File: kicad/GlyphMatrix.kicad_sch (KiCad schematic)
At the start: 36 parts, among them J1 Conn_01x04, SW1 SW_Push, SW2 SW_Push, U1 W25Q128JVS, U2 USBLC6-2SC6, U3 XC6206PxxxMR-Regulator_Linear, Y1 12MHz

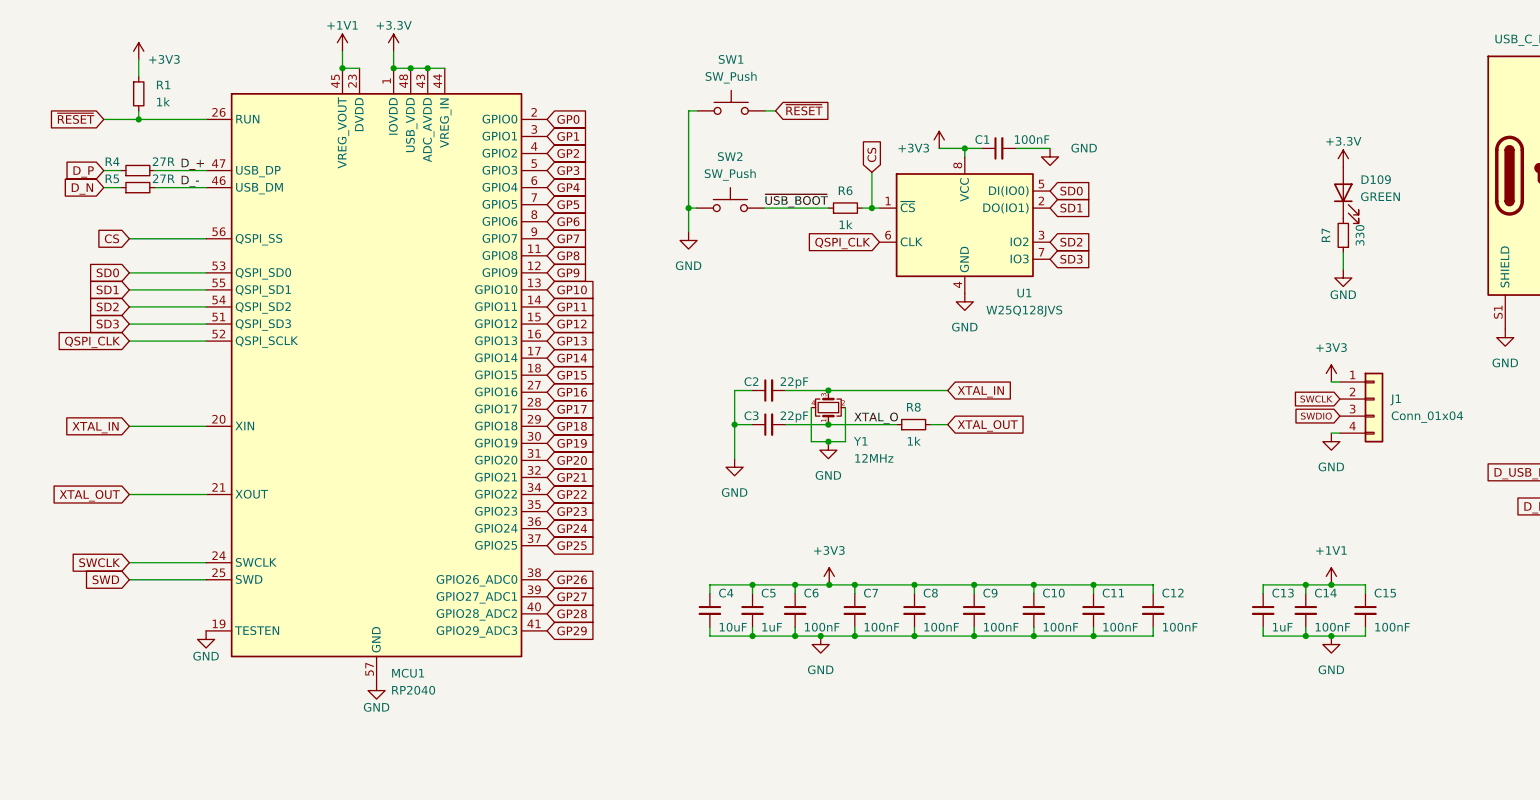
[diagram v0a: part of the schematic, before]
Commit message: added MCU
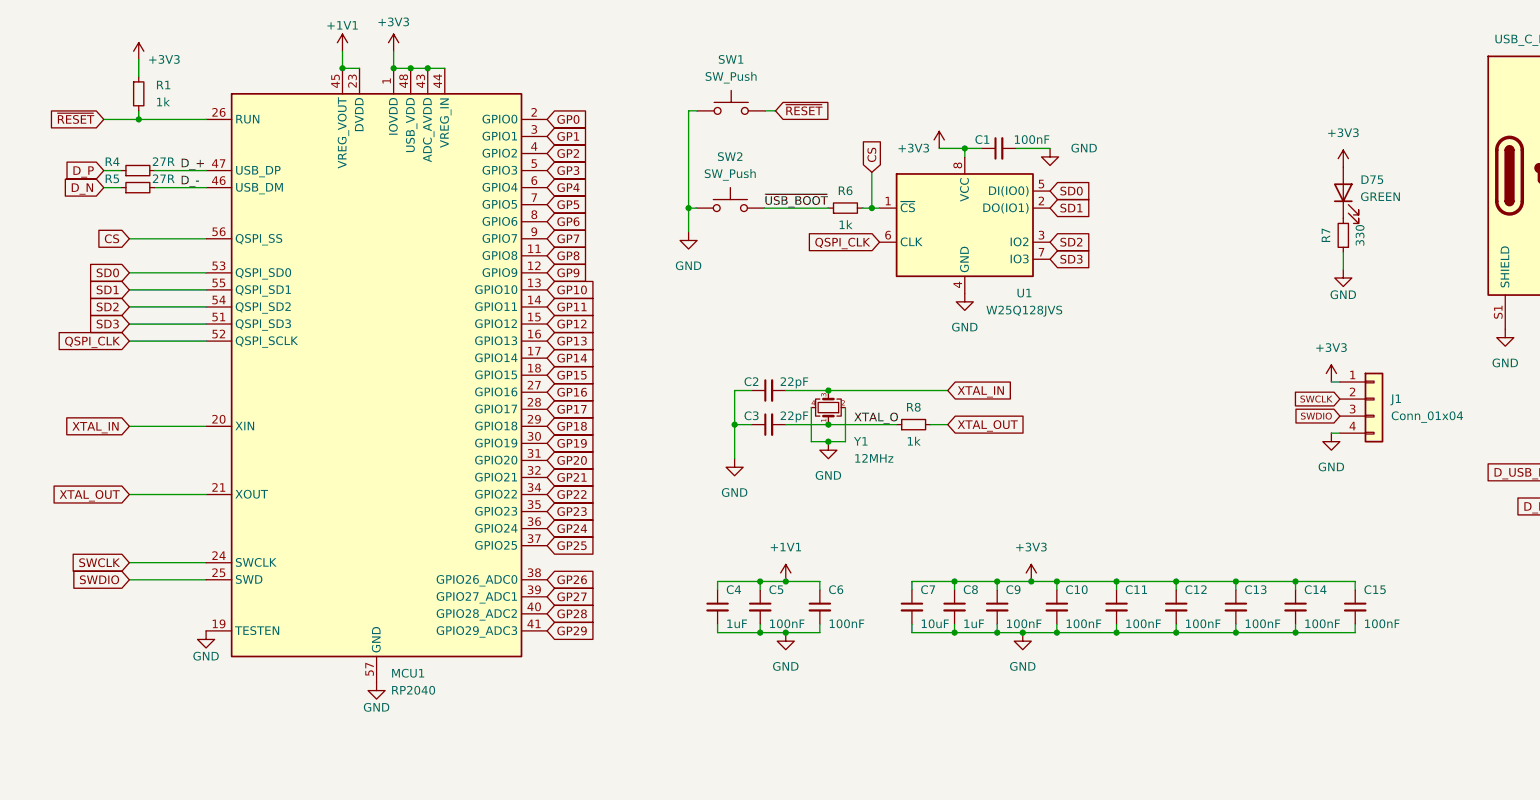
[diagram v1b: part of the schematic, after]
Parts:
- renumbered C7 to C10, C8 to C11, C9 to C12, C10 to C13, C11 to C14, C12 to C15, C13 to C4, C14 to C5, C15 to C6, C4 to C7, C5 to C8, C6 to C9, D109 to D75
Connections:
- net +3.3V is gone; now on net +3V3: D75.2 (A), MCU1.1 (IOVDD), MCU1.10 (IOVDD), MCU1.22 (IOVDD), MCU1.33 (IOVDD), MCU1.42 (IOVDD), MCU1.43 (ADC_AVDD), MCU1.44 (VREG_IN), MCU1.48 (USB_VDD), MCU1.49 (IOVDD)
- net SWD is gone; now on net SWDIO: MCU1.25 (SWD)
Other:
- moved on the sheet: C10, C11, C12, C13, C14, C15, C4, C5, C6, C7, C8, C9

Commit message: pogo pin connectors
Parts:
- renumbered D75 to LED1
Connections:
- net GP0 renamed SCR
- net GP1 renamed NUM
- net GP10 renamed ROW04
- net GP11 renamed ROW03
- net GP12 renamed ROW02
- net GP13 renamed ROW01
- net GP14 renamed ROW00
- net GP15 renamed CAPS
- net GP16 renamed COL0
- net GP17 renamed COL1
- net GP18 renamed COL2
- net GP19 renamed COL3
- net GP2 renamed ROW17
- net GP20 renamed COL4
- net GP21 renamed COL5
- net GP22 renamed COL6
- net GP23 renamed ROW06
- net GP24 renamed ROW07
- net GP25 renamed ROW08
- net GP26 renamed ROW09
- net GP27 renamed ROW10
- net GP28 renamed ROW11
- net GP3 renamed ROW16
- net GP4 renamed ROW15
- net GP5 renamed ROW14
- net GP6 renamed ROW13
- net GP7 renamed ROW12
- net GP8 renamed RGB
- net GP9 renamed ROW05
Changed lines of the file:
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@@
 		)
 	)
-	(global_label "GP17"
+	(global_label "COL1"
 		(shape input)
 		(at 88.392 77.978 0)
@@
 		)
 		(property "Intersheetrefs" "${INTERSHEET_REFS}"
-			(at 94.8885 77.978 0)
+			(at 96.2153 77.978 0)
 			(effects
 				(font
@@
 		)
 	)
-	(global_label "GP8"
+	(global_label "RGB"
 		(shape input)
 		(at 88.392 55.118 0)
@@
 		)
 		(property "Intersheetrefs" "${INTERSHEET_REFS}"
-			(at 94.8885 55.118 0)
+			(at 95.1872 55.118 0)
 			(effects
 				(font
@@
 		)
 	)
-	(global_label "GP16"
+	(global_label "COL0"
 		(shape input)
 		(at 88.392 75.438 0)
@@
 		)
 		(property "Intersheetrefs" "${INTERSHEET_REFS}"
-			(at 94.8885 75.438 0)
+			(at 96.2153 75.438 0)
 			(effects
 				(font
@@
 		)
 	)
-	(global_label "GP6"
+	(global_label "ROW13"
 		(shape input)
 		(at 88.392 50.038 0)
@@
 		)
 		(property "Intersheetrefs" "${INTERSHEET_REFS}"
-			(at 94.8885 50.038 0)
+			(at 97.8481 50.038 0)
 			(effects
 				(font
@@
 		)
 	)
-	(global_label "GP13"
+	(global_label "ROW01"
 		(shape input)
 		(at 88.392 67.818 0)
@@
 		)
 		(property "Intersheetrefs" "${INTERSHEET_REFS}"
-			(at 94.8885 67.818 0)
+			(at 97.8481 67.818 0)
 			(effects
 				(font
@@
 		)
 	)
-	(global_label "GP20"
+	(global_label "COL4"
 		(shape input)
 		(at 88.392 85.598 0)
@@
 		)
 		(property "Intersheetrefs" "${INTERSHEET_REFS}"
-			(at 94.8885 85.598 0)
+			(at 96.2153 85.598 0)
 			(effects
 				(font
@@
 		)
 	)
-	(global_label "GP25"
+	(global_label "ROW08"
 		(shape input)
 		(at 88.392 98.298 0)
@@
 		)
 		(property "Intersheetrefs" "${INTERSHEET_REFS}"
-			(at 94.8885 98.298 0)
+			(at 97.8481 98.298 0)
 			(effects
 				(font
@@
 		)
 	)
-	(global_label "GP2"
+	(global_label "ROW17"
 		(shape input)
 		(at 88.392 39.878 0)
@@
 		)
 		(property "Intersheetrefs" "${INTERSHEET_REFS}"
-			(at 94.8885 39.878 0)
+			(at 97.8481 39.878 0)
 			(effects
 				(font
@@
 		)
 	)
-	(global_label "GP0"
+	(global_label "SCR"
 		(shape input)
 		(at 88.392 34.798 0)
@@
 		)
 		(property "Intersheetrefs" "${INTERSHEET_REFS}"
-			(at 94.8885 34.798 0)
+			(at 95.1267 34.798 0)
 			(effects
 				(font
@@
 		)
 	)
-	(global_label "GP24"
+	(global_label "ROW07"
 		(shape input)
 		(at 88.392 95.758 0)
@@
 		)
 		(property "Intersheetrefs" "${INTERSHEET_REFS}"
-			(at 94.8885 95.758 0)
+			(at 97.8481 95.758 0)
 			(effects
 				(font
@@
 		)
 	)
-	(global_label "GP14"
+	(global_label "ROW00"
 		(shape input)
 		(at 88.392 70.358 0)
@@
 		)
 		(property "Intersheetrefs" "${INTERSHEET_REFS}"
-			(at 94.8885 70.358 0)
+			(at 97.8481 70.358 0)
 			(effects
 				(font
@@
 		)
 	)
-	(global_label "GP9"
+	(global_label "ROW05"
 		(shape input)
 		(at 88.392 57.658 0)
@@
 		)
 		(property "Intersheetrefs" "${INTERSHEET_REFS}"
-			(at 94.8885 57.658 0)
+			(at 97.8481 57.658 0)
 			(effects
 				(font
@@
 		)
 	)
-	(global_label "GP23"
+	(global_label "ROW06"
 		(shape input)
 		(at 88.392 93.218 0)
@@
 		)
 		(property "Intersheetrefs" "${INTERSHEET_REFS}"
-			(at 94.8885 93.218 0)
+			(at 97.8481 93.218 0)
 			(effects
 				(font
@@
 		)
 	)
-	(global_label "GP15"
+	(global_label "CAPS"
 		(shape input)
 		(at 88.392 72.898 0)
@@
 		)
 		(property "Intersheetrefs" "${INTERSHEET_REFS}"
-			(at 94.8885 72.898 0)
+			(at 96.2153 72.898 0)
 			(effects
 				(font
@@
 		)
 	)
-	(global_label "GP28"
+	(global_label "ROW11"
 		(shape input)
 		(at 88.392 108.458 0)
@@
 		)
 		(property "Intersheetrefs" "${INTERSHEET_REFS}"
-			(at 94.8885 108.458 0)
+			(at 97.8481 108.458 0)
 			(effects
 				(font
@@
 		)
 	)
-	(global_label "GP19"
+	(global_label "COL3"
 		(shape input)
 		(at 88.392 83.058 0)
@@
 		)
 		(property "Intersheetrefs" "${INTERSHEET_REFS}"
-			(at 94.8885 83.058 0)
+			(at 96.2153 83.058 0)
 			(effects
 				(font
@@
 		)
 	)
-	(global_label "GP10"
+	(global_label "ROW04"
 		(shape input)
 		(at 88.392 60.198 0)
@@
 		)
 		(property "Intersheetrefs" "${INTERSHEET_REFS}"
-			(at 94.8885 60.198 0)
+			(at 97.8481 60.198 0)
 			(effects
 				(font
@@
 		)
 	)
-	(global_label "GP11"
+	(global_label "ROW03"
 		(shape input)
 		(at 88.392 62.738 0)
@@
 		)
 		(property "Intersheetrefs" "${INTERSHEET_REFS}"
-			(at 94.8885 62.738 0)
+			(at 97.8481 62.738 0)
 			(effects
 				(font
@@
 		)
 	)
-	(global_label "GP7"
+	(global_label "ROW12"
 		(shape input)
 		(at 88.392 52.578 0)
@@
 		)
 		(property "Intersheetrefs" "${INTERSHEET_REFS}"
-			(at 94.8885 52.578 0)
+			(at 97.8481 52.578 0)
 			(effects
 				(font
@@
 		)
 	)
-	(global_label "GP27"
+	(global_label "ROW10"
 		(shape input)
 		(at 88.392 105.918 0)
@@
 		)
 		(property "Intersheetrefs" "${INTERSHEET_REFS}"
-			(at 94.8885 105.918 0)
+			(at 97.8481 105.918 0)
 			(effects
 				(font
@@
 		)
 	)
-	(global_label "GP1"
+	(global_label "NUM"
 		(shape input)
 		(at 88.392 37.338 0)
@@
 		)
 		(property "Intersheetrefs" "${INTERSHEET_REFS}"
-			(at 94.8885 37.338 0)
+			(at 95.4896 37.338 0)
 			(effects
 				(font
@@
 		)
 	)
-	(global_label "GP3"
+	(global_label "ROW16"
 		(shape input)
 		(at 88.392 42.418 0)
@@
 		)
 		(property "Intersheetrefs" "${INTERSHEET_REFS}"
-			(at 94.8885 42.418 0)
+			(at 97.8481 42.418 0)
 			(effects
 				(font
@@
 		)
 	)
-	(global_label "GP4"
+	(global_label "ROW15"
 		(shape input)
 		(at 88.392 44.958 0)
@@
 		)
 		(property "Intersheetrefs" "${INTERSHEET_REFS}"
-			(at 94.8885 44.958 0)
+			(at 97.8481 44.958 0)
 			(effects
 				(font
@@
 		)
 	)
-	(global_label "GP21"
+	(global_label "COL5"
 		(shape input)
 		(at 88.392 88.138 0)
@@
 		)
 		(property "Intersheetrefs" "${INTERSHEET_REFS}"
-			(at 94.8885 88.138 0)
+			(at 96.2153 88.138 0)
 			(effects
 				(font
@@
 		)
 	)
-	(global_label "GP26"
+	(global_label "ROW09"
 		(shape input)
 		(at 88.392 103.378 0)
@@
 		)
 		(property "Intersheetrefs" "${INTERSHEET_REFS}"
-			(at 94.8885 103.378 0)
+			(at 97.8481 103.378 0)
 			(effects
 				(font
@@
 		)
 	)
-	(global_label "GP5"
+	(global_label "ROW14"
 		(shape input)
 		(at 88.392 47.498 0)
@@
 		)
 		(property "Intersheetrefs" "${INTERSHEET_REFS}"
-			(at 94.8885 47.498 0)
+			(at 97.8481 47.498 0)
 			(effects
 				(font
@@
 		)
 	)
-	(global_label "GP18"
+	(global_label "COL2"
 		(shape input)
 		(at 88.392 80.518 0)
@@
 		)
 		(property "Intersheetrefs" "${INTERSHEET_REFS}"
-			(at 94.8885 80.518 0)
+			(at 96.2153 80.518 0)
 			(effects
 				(font
@@
 		)
 	)
-	(global_label "GP22"
+	(global_label "COL6"
 		(shape input)
 		(at 88.392 90.678 0)
@@
 		)
 		(property "Intersheetrefs" "${INTERSHEET_REFS}"
-			(at 94.8885 90.678 0)
+			(at 96.2153 90.678 0)
 			(effects
 				(font
@@
 		)
 	)
-	(global_label "GP12"
+	(global_label "ROW02"
 		(shape input)
 		(at 88.392 65.278 0)
@@
 		)
 		(property "Intersheetrefs" "${INTERSHEET_REFS}"
-			(at 94.8885 65.278 0)
+			(at 97.8481 65.278 0)
 			(effects
 				(font
@@
 		(on_board yes)
 		(dnp no)
-		(property "Reference" "D75"
+		(property "Reference" "LED1"
 			(at 209.55 43.815 90)
 			(effects
@@
 			(project "OmniCode"
 				(path "/c7177d09-71a2-4de7-9a3e-bfc16a7f2797"
-					(reference "D75")
+					(reference "LED1")
 					(unit 1)
 				)

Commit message: screw holes
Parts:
- LED1: value GREEN -> WHITE
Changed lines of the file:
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@@
 			)
 		)
-		(property "Value" "GREEN"
+		(property "Value" "WHITE"
 			(at 209.55 46.355 90)
 			(effects

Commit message: artwork
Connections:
- net CAPS: now also MCU1.11 (GPIO8); no longer MCU1.18 (GPIO15)
- net NUM: now also MCU1.9 (GPIO7); no longer MCU1.3 (GPIO1)
- net RGB: now also MCU1.16 (GPIO13); no longer MCU1.11 (GPIO8)
- net ROW00: now also MCU1.12 (GPIO9); no longer MCU1.17 (GPIO14)
- net ROW01: now also MCU1.13 (GPIO10); no longer MCU1.16 (GPIO13)
- net ROW02: now also MCU1.14 (GPIO11); no longer MCU1.15 (GPIO12)
- net ROW03: now also MCU1.18 (GPIO15); no longer MCU1.14 (GPIO11)
- net ROW04: now also MCU1.17 (GPIO14); no longer MCU1.13 (GPIO10)
- net ROW05: now also MCU1.15 (GPIO12); no longer MCU1.12 (GPIO9)
- net ROW12: now also MCU1.7 (GPIO5); no longer MCU1.9 (GPIO7)
- net ROW13: now also MCU1.6 (GPIO4); no longer MCU1.8 (GPIO6)
- net ROW14: now also MCU1.5 (GPIO3); no longer MCU1.7 (GPIO5)
- net ROW15: now also MCU1.4 (GPIO2); no longer MCU1.6 (GPIO4)
- net ROW16: now also MCU1.3 (GPIO1); no longer MCU1.5 (GPIO3)
- net ROW17: now also MCU1.2 (GPIO0); no longer MCU1.4 (GPIO2)
- net SCR: now also MCU1.8 (GPIO6); no longer MCU1.2 (GPIO0)
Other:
- added sheet RGB (GlyphMatrix-RGB.kicad_sch)
- title: (none) -> RP2040 - Keyboard: OmniCode:9001

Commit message: artwork #2
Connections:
- net COL4: now also MCU1.34 (GPIO22); no longer MCU1.31 (GPIO20)
- net COL6: now also MCU1.31 (GPIO20); no longer MCU1.34 (GPIO22)
- net ROW12: now also MCU1.2 (GPIO0); no longer MCU1.7 (GPIO5)
- net ROW13: now also MCU1.3 (GPIO1); no longer MCU1.6 (GPIO4)
- net ROW14: now also MCU1.4 (GPIO2); no longer MCU1.5 (GPIO3)
- net ROW15: now also MCU1.5 (GPIO3); no longer MCU1.4 (GPIO2)
- net ROW16: now also MCU1.6 (GPIO4); no longer MCU1.3 (GPIO1)
- net ROW17: now also MCU1.7 (GPIO5); no longer MCU1.2 (GPIO0)

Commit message: kibot
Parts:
- LED1: LCSC C84264 -> C965808
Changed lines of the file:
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@@
 			)
 		)
-		(property "LCSC" "C84264"
+		(property "LCSC" "C965808"
 			(at 209.55 43.815 0)
 			(effects

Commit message: reorg schematic (#18)
* GlyphMatrix

* PhaseShift

* DeltaForm
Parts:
- removed C1, C10, C11, C12, C13, C14, C15, C5, C6, C9: 100nF, Capacitor_SMD:C_0402_1005Metric, symbol Device:C_Small
- removed C16, C17, C4, C8: 1uF, Capacitor_SMD:C_0402_1005Metric, symbol Device:C_Small
- removed C2, C3: 22pF, Capacitor_SMD:C_0402_1005Metric, symbol Device:C_Small
- removed C7: 10uF, Capacitor_SMD:C_0402_1005Metric, symbol Device:C_Small
- removed F1: 500mA, Fuse:Fuse_1206_3216Metric, symbol Device:Polyfuse_Small
- removed J1: Conn_01x04, Connector_PinHeader_2.00mm:PinHeader_2x02_P2.00mm_Vertical_SMD, symbol Connector_Generic:Conn_01x04
- removed LED1: WHITE, LED_SMD:LED_0603_1608Metric_Pad1.05x0.95mm_HandSolder, symbol Device:LED
- removed MCU1: RP2040, TB2086_SMD_G:RP2040-QFN-56, symbol MCU_RaspberryPi:RP2040
- removed R1, R6, R8: 1k, Resistor_SMD:R_0402_1005Metric, symbol Device:R_Small
- removed R2, R3: 5k1, Resistor_SMD:R_0402_1005Metric, symbol Device:R_Small
- removed R4, R5: 27R, Resistor_SMD:R_0603_1608Metric, symbol Device:R_Small
- removed R7: 330, Resistor_SMD:R_0603_1608Metric, symbol Device:R_Small
- removed SW1, SW2: SW_Push, Button_Switch_SMD:SW_SPST_SKQG_WithoutStem, symbol Switch:SW_Push
- removed U1: W25Q128JVS, Package_SO:SOIC-8_5.3x5.3mm_P1.27mm, symbol Memory_Flash:W25Q128JVS
- removed U2: USBLC6-2SC6, Package_TO_SOT_SMD:SOT-23-6, symbol Power_Protection:USBLC6-2SC6
- removed U3: XC6206PxxxMR-Regulator_Linear, Package_TO_SOT_SMD:SOT-23, symbol kicad-keyboard-parts:XC6206PxxxMR-Regulator_Linear
- removed USB1: USB_C_Receptacle_USB2.0, TB2086_SMD:GCT_USB4520-03-0-A_REVA, symbol Connector:USB_C_Receptacle_USB2.0
- removed Y1: 12MHz, Crystal:Crystal_SMD_3225-4Pin_3.2x2.5mm, symbol Device:Crystal_GND24_Small
- added D1, D10, D11, D12, D13, D14, D15, D16, D17, D18, D19, D2, D20, D21, D22, D23, D24, D25, D26, D27, D28, D29, D3, D30, D31, D32, D33, D34, D35, D36, D37, D38, D39, D4, D40, D41, D42, D43, D44, D45, D46, D47, D48, D49, D5, D50, D51, D52, D53, D54, D55, D56, D57, D58, D59, D6, D60, D61, D62, D63, D64, D65, D66, D67, D68, D69, D7, D70, D71, D72, D73, D74, D8, D9: 1N4148W, TB2086_SMD:D3_SMD, symbol Device:D
- added H1, H2, H3, H4, H5, H6, H7, H8: MountingHole_Pad, TB2086_MISC:MountingHole_2.2mm_M2_Pad, symbol TB2086_MISC:MountingHole_Pad
- added LED2: GREEN, LED_SMD:LED_0603_1608Metric_Pad1.05x0.95mm_HandSolder, symbol Device:LED
- added POGO1, POGO2: Conn_01x05, TB2086_MISC:Pogopin_1x05_P2.54mm_Curved, symbol Connector_Generic:Conn_01x05
- added POGO3, POGO4, POGO5, POGO6: Conn_01x07, TB2086_MISC:Pogopin_1x07_P2.54mm_Curved, symbol Connector_Generic:Conn_01x07
- added R9: 330, Resistor_SMD:R_0603_1608Metric, symbol Device:R_Small
- added S1, S10, S11, S12, S13, S14, S15, S16, S17, S18, S19, S2, S20, S21, S22, S23, S24, S25, S26, S27, S28, S29, S3, S30, S31, S32, S33, S34, S35, S36, S37, S38, S39, S4, S40, S41, S42, S43, S44, S45, S46, S47, S48, S49, S5, S50, S51, S52, S53, S54, S55, S56, S57, S58, S59, S6, S60, S61, S62, S63, S7, S8, S9: SW_MX_HS, TB2086_KEYSWITCH:SW_MX_HS_1u, symbol TB2086_KEYSWITCH:SW_MX_HS
- added S64: SW_MX_HS, TB2086_KEYSWITCH:SW_MX_HS_1.25u, symbol TB2086_KEYSWITCH:SW_MX_HS
- added S65, S66: SW_MX_HS, TB2086_KEYSWITCH:SW_MX_HS_1.5u, symbol TB2086_KEYSWITCH:SW_MX_HS
- added S67, S68, S69: SW_MX_HS, TB2086_KEYSWITCH:SW_MX_HS_1.75u, symbol TB2086_KEYSWITCH:SW_MX_HS
- added S70: SW_MX_HS, TB2086_KEYSWITCH:SW_MX_HS_2u, symbol TB2086_KEYSWITCH:SW_MX_HS
- added S71, S72: SW_MX_HS, TB2086_KEYSWITCH:SW_MX_HS_2.25u, symbol TB2086_KEYSWITCH:SW_MX_HS
- added S73: SW_MX_HS, TB2086_KEYSWITCH:SW_MX_HS_2.75u, symbol TB2086_KEYSWITCH:SW_MX_HS
- added S74: SW_MX_HS, TB2086_KEYSWITCH:SW_MX_HS_6.25u, symbol TB2086_KEYSWITCH:SW_MX_HS
- added STB1, STB2, STB3, STB4: Stabilizer_Cherry_MX_2.00u, Stabilizer_Cherry_MX_2.00u, symbol PCM_marbastlib-mx:MX_stab
- added STB5: Stabilizer_Cherry_MX_6.25u, Stabilizer_Cherry_MX_6.25u, symbol PCM_marbastlib-mx:MX_stab
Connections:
- net +5V: now also POGO1.4 (Pin_4), POGO2.2 (Pin_2)
- net CAPS: now also LED2.2 (A)
- net COL0: now also POGO3.1 (Pin_1), POGO4.7 (Pin_7), S1.2, S13.2, S14.2, S65.2, S66.2, S67.2, S68.2, S69.2, S70.2, S71.2, S72.2, S73.2
- net COL1: now also POGO3.2 (Pin_2), POGO4.6 (Pin_6), S12.2, S15.2, S26.2, S27.2, S38.2, S39.2, S50.2, S60.2
- net COL2: now also POGO3.3 (Pin_3), POGO4.5 (Pin_5), S11.2, S16.2, S2.2, S25.2, S28.2, S37.2, S40.2, S49.2, S51.2, S63.2, S64.2
- net COL3: now also POGO3.4 (Pin_4), POGO4.4 (Pin_4), S10.2, S17.2, S24.2, S29.2, S3.2, S36.2, S41.2, S48.2, S52.2, S59.2, S62.2
- net COL4: now also POGO3.7 (Pin_7), POGO4.1 (Pin_1), S18.2, S23.2, S30.2, S35.2, S4.2, S42.2, S47.2, S53.2, S58.2, S61.2, S9.2
- net COL5: now also POGO3.6 (Pin_6), POGO4.2 (Pin_2), S19.2, S22.2, S31.2, S34.2, S43.2, S46.2, S5.2, S54.2, S57.2, S74.2, S8.2
- net COL6: now also POGO3.5 (Pin_5), POGO4.3 (Pin_3), S20.2, S21.2, S32.2, S33.2, S44.2, S45.2, S55.2, S56.2, S6.2, S7.2
- net GND: now also H1.1, H2.1, H3.1, H4.1, H5.1, H6.1, H7.1, H8.1, POGO1.5 (Pin_5), POGO2.1 (Pin_1), R9.1
- net NUM: now also POGO1.3 (Pin_3), POGO2.3 (Pin_3)
- net ROW00: now also D1.1 (K), D2.1 (K), D3.1 (K), D4.1 (K), D5.1 (K), D6.1 (K)
- net ROW01: now also D14.1 (K), D15.1 (K), D16.1 (K), D17.1 (K), D18.1 (K), D19.1 (K), D20.1 (K)
- net ROW02: now also D27.1 (K), D28.1 (K), D29.1 (K), D30.1 (K), D31.1 (K), D32.1 (K), D65.1 (K)
- net ROW03: now also D39.1 (K), D40.1 (K), D41.1 (K), D42.1 (K), D43.1 (K), D44.1 (K), D67.1 (K)
- net ROW04: now also D50.1 (K), D51.1 (K), D52.1 (K), D53.1 (K), D54.1 (K), D55.1 (K), D72.1 (K)
- net ROW05: now also D60.1 (K), D64.1 (K), D68.1 (K), D74.1 (K)
- net ROW06: now also D10.1 (K), D11.1 (K), D12.1 (K), D13.1 (K), D7.1 (K), D8.1 (K), D9.1 (K)
- net ROW07: now also D21.1 (K), D22.1 (K), D23.1 (K), D24.1 (K), D25.1 (K), D26.1 (K), D70.1 (K)
- net ROW08: now also D33.1 (K), D34.1 (K), D35.1 (K), D36.1 (K), D37.1 (K), D38.1 (K), D66.1 (K)
- net ROW09: now also D45.1 (K), D46.1 (K), D47.1 (K), D48.1 (K), D49.1 (K), D71.1 (K)
- net ROW10: now also D56.1 (K), D57.1 (K), D58.1 (K), D59.1 (K), D73.1 (K)
- net ROW11: now also D61.1 (K), D62.1 (K), D63.1 (K), D69.1 (K)
- net ROW12: now also POGO5.1 (Pin_1), POGO6.7 (Pin_7)
- net ROW13: now also POGO5.2 (Pin_2), POGO6.6 (Pin_6)
- net ROW14: now also POGO5.3 (Pin_3), POGO6.5 (Pin_5)
- net ROW15: now also POGO5.4 (Pin_4), POGO6.4 (Pin_4)
- net ROW16: now also POGO5.5 (Pin_5), POGO6.3 (Pin_3)
- net ROW17: now also POGO5.6 (Pin_6), POGO6.2 (Pin_2)
- net SCR: now also POGO1.2 (Pin_2), POGO2.4 (Pin_4)
- new net: D23.2 (A), S23.1
- new net: D21.2 (A), S21.1
- new net: D34.2 (A), S34.1
- new net: D30.2 (A), S30.1
- new net: D11.2 (A), S11.1
- new net: D27.2 (A), S27.1
- new net: D2.2 (A), S2.1
- new net: D63.2 (A), S63.1
- new net: D71.2 (A), S71.1
- new net: D16.2 (A), S16.1
- new net: D66.2 (A), S66.1
- new net: D41.2 (A), S41.1
- new net: D39.2 (A), S39.1
- new net: D69.2 (A), S69.1
- new net: D19.2 (A), S19.1
- new net: D32.2 (A), S32.1
- new net: D46.2 (A), S46.1
- new net: D53.2 (A), S53.1
- new net: D54.2 (A), S54.1
- new net: D26.2 (A), S26.1
- new net: D59.2 (A), S59.1
- new net: D14.2 (A), S14.1
- new net: D9.2 (A), S9.1
- new net: D15.2 (A), S15.1
- new net: D67.2 (A), S67.1
- new net: D64.2 (A), S64.1
- new net: D73.2 (A), S73.1
- new net: D60.2 (A), S60.1
- new net: D50.2 (A), S50.1
- new net: D44.2 (A), S44.1
- new net: D37.2 (A), S37.1
- new net: D25.2 (A), S25.1
- new net: D72.2 (A), S72.1
- new net: D40.2 (A), S40.1
- new net: D70.2 (A), S70.1
- new net: D20.2 (A), S20.1
- new net: D45.2 (A), S45.1
- new net: D57.2 (A), S57.1
- new net: LED2.1 (K), R9.2
- new net: D74.2 (A), S74.1
- new net: D55.2 (A), S55.1
- new net: D10.2 (A), S10.1
- new net: D43.2 (A), S43.1
- new net: D28.2 (A), S28.1
- new net: D31.2 (A), S31.1
- new net: D29.2 (A), S29.1
- new net: D22.2 (A), S22.1
- new net: D52.2 (A), S52.1
- new net: D68.2 (A), S68.1
- new net: D56.2 (A), S56.1
- new net: D61.2 (A), S61.1
- new net: D4.2 (A), S4.1
- new net: D38.2 (A), S38.1
- new net: D58.2 (A), S58.1
- new net: D13.2 (A), S13.1
- new net: D36.2 (A), S36.1
- new net: D12.2 (A), S12.1
- new net: D49.2 (A), S49.1
- new net: D33.2 (A), S33.1
- new net: D6.2 (A), S6.1
- new net: D51.2 (A), S51.1
- new net: D3.2 (A), S3.1
- new net: D42.2 (A), S42.1
- new net: D7.2 (A), S7.1
- new net: D18.2 (A), S18.1
- new net: D5.2 (A), S5.1
- new net: D35.2 (A), S35.1
- new net: D47.2 (A), S47.1
- new net: D65.2 (A), S65.1
- new net: D48.2 (A), S48.1
- new net: D24.2 (A), S24.1
- new net: D8.2 (A), S8.1
- new net: D62.2 (A), S62.1
- new net: D17.2 (A), S17.1
- new net: D1.2 (A), S1.1
- new net RGB_FOM_LEFT: POGO1.1 (Pin_1)
- new net RGB_FOM_RIGHT: POGO6.1 (Pin_1)
- new net RGB_TO_LEFT: POGO5.7 (Pin_7)
- new net RGB_TO_RIGHT: POGO2.5 (Pin_5)
- no-connect marks 2 -> 0
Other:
- removed sheet GlyphMatrix
- added sheet RP2040 (GlyphMatrix-RP2040.kicad_sch)

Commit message: updated schematic for GlyphMatrix (#20)
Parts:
- removed LED2: GREEN, LED_SMD:LED_0603_1608Metric_Pad1.05x0.95mm_HandSolder, symbol Device:LED
- removed R9: 330, Resistor_SMD:R_0603_1608Metric, symbol Device:R_Small
